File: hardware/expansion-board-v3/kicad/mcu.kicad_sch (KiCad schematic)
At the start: 31 parts, among them J4 USB-C_16P, SW1 RESET短接焊盘, SW2 BOOTSEL短接焊盘, U8 RP2040, U9 W25Q128JVSIQ, Y1 12MHz

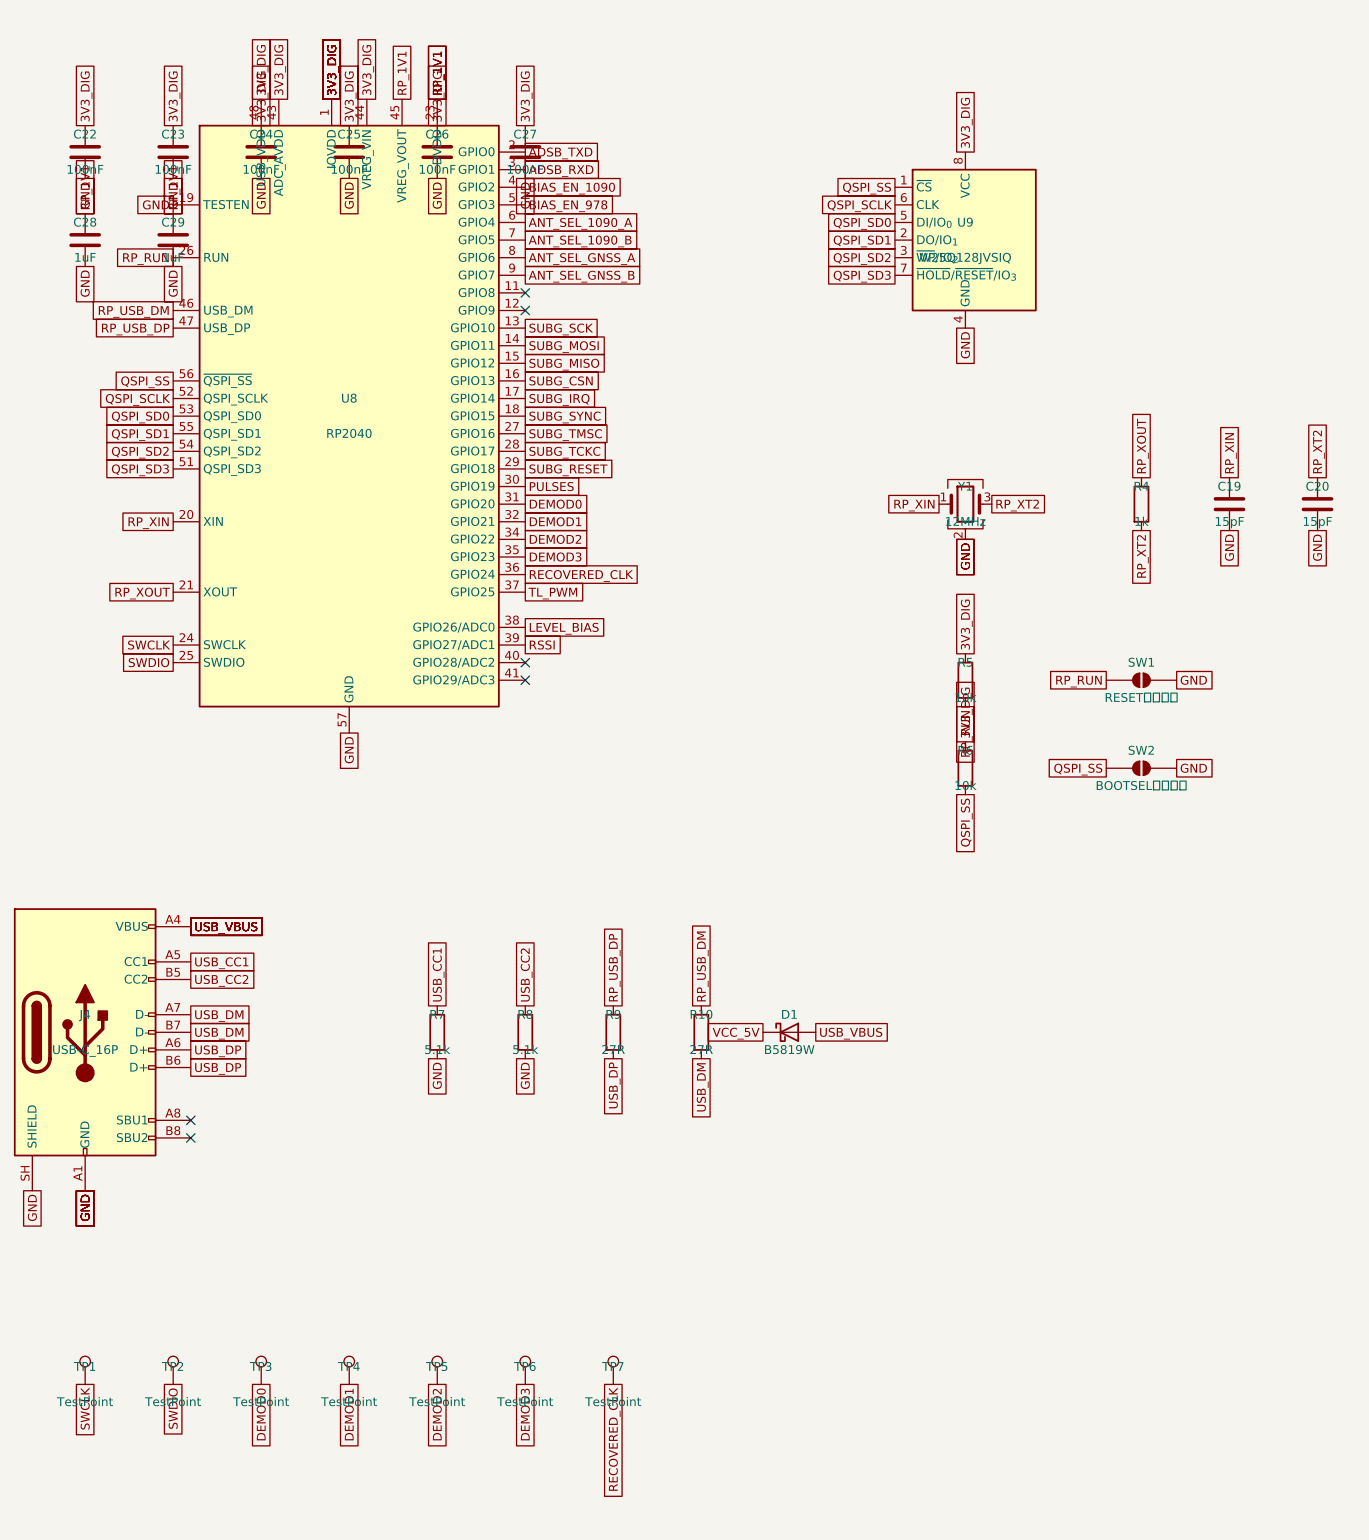
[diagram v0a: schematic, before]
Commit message: feat(v3): backport V4 fixes into a clean V3.9 candidate (phases A-D)
Builds the V3.9 candidate from the V3.8 master rather than from the
working-tree intermediate. The intermediate had the 14 audit parts and a
cleared back side, but had lost 24 board-level silkscreen strings and all
four named RF zones - tools/rebuild.sh starts with gen_pcb.py, which calls
pcbnew.NewBoard(), and neither gr_text nor named zones live in
PLACEMENT.py or ROUTES.json, so every run drops them. The master is the
opposite: intact silkscreen and zones, missing only components. Adding
components back is enumerable (14 designators); restoring 24 silkscreen
strings with correct position, layer, size and mirroring is not.

Coordinates are transplanted from the intermediate, so nothing is
re-placed by hand. What that does cost is copper: the master was routed
without these parts, and 13 of the 18 land on existing tracks. Ripping
those out plus the resulting dangling chains removes 176 segments and 26
vias against the master's 1620/377 - all of it folded into phase E, which
was going to be manual routing anyway. Re-placing 13 parts on a fully
routed board would have been worse; C82-C86 are RP2040 local decouplers
that must stay next to the die, which is exactly how V4.3 ended up with
its 30 mm detour.

Phase B removes the AD8319 experimental branch (U13, R20, DET_TADJ). The
"directional error" turned out to reach into the generators, not just
prose - five places, of which two would have produced wrong hardware:

    gen_bom_smt.py   SKIP_REF = {"U14"}   the only detector excluded
                                          from the pick-and-place BOM
    gen_bom.py       ORDERED listed "AD8313ARMZ(备,二选一)", a suffixed
                     string that never matched the netlist value, so the
                     part had never once been classified

Ordering the V3.8 BOM as it stood would have produced a board whose 1090
receive chain has no detector at all. Phase B's hard criterion now holds:
excluding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
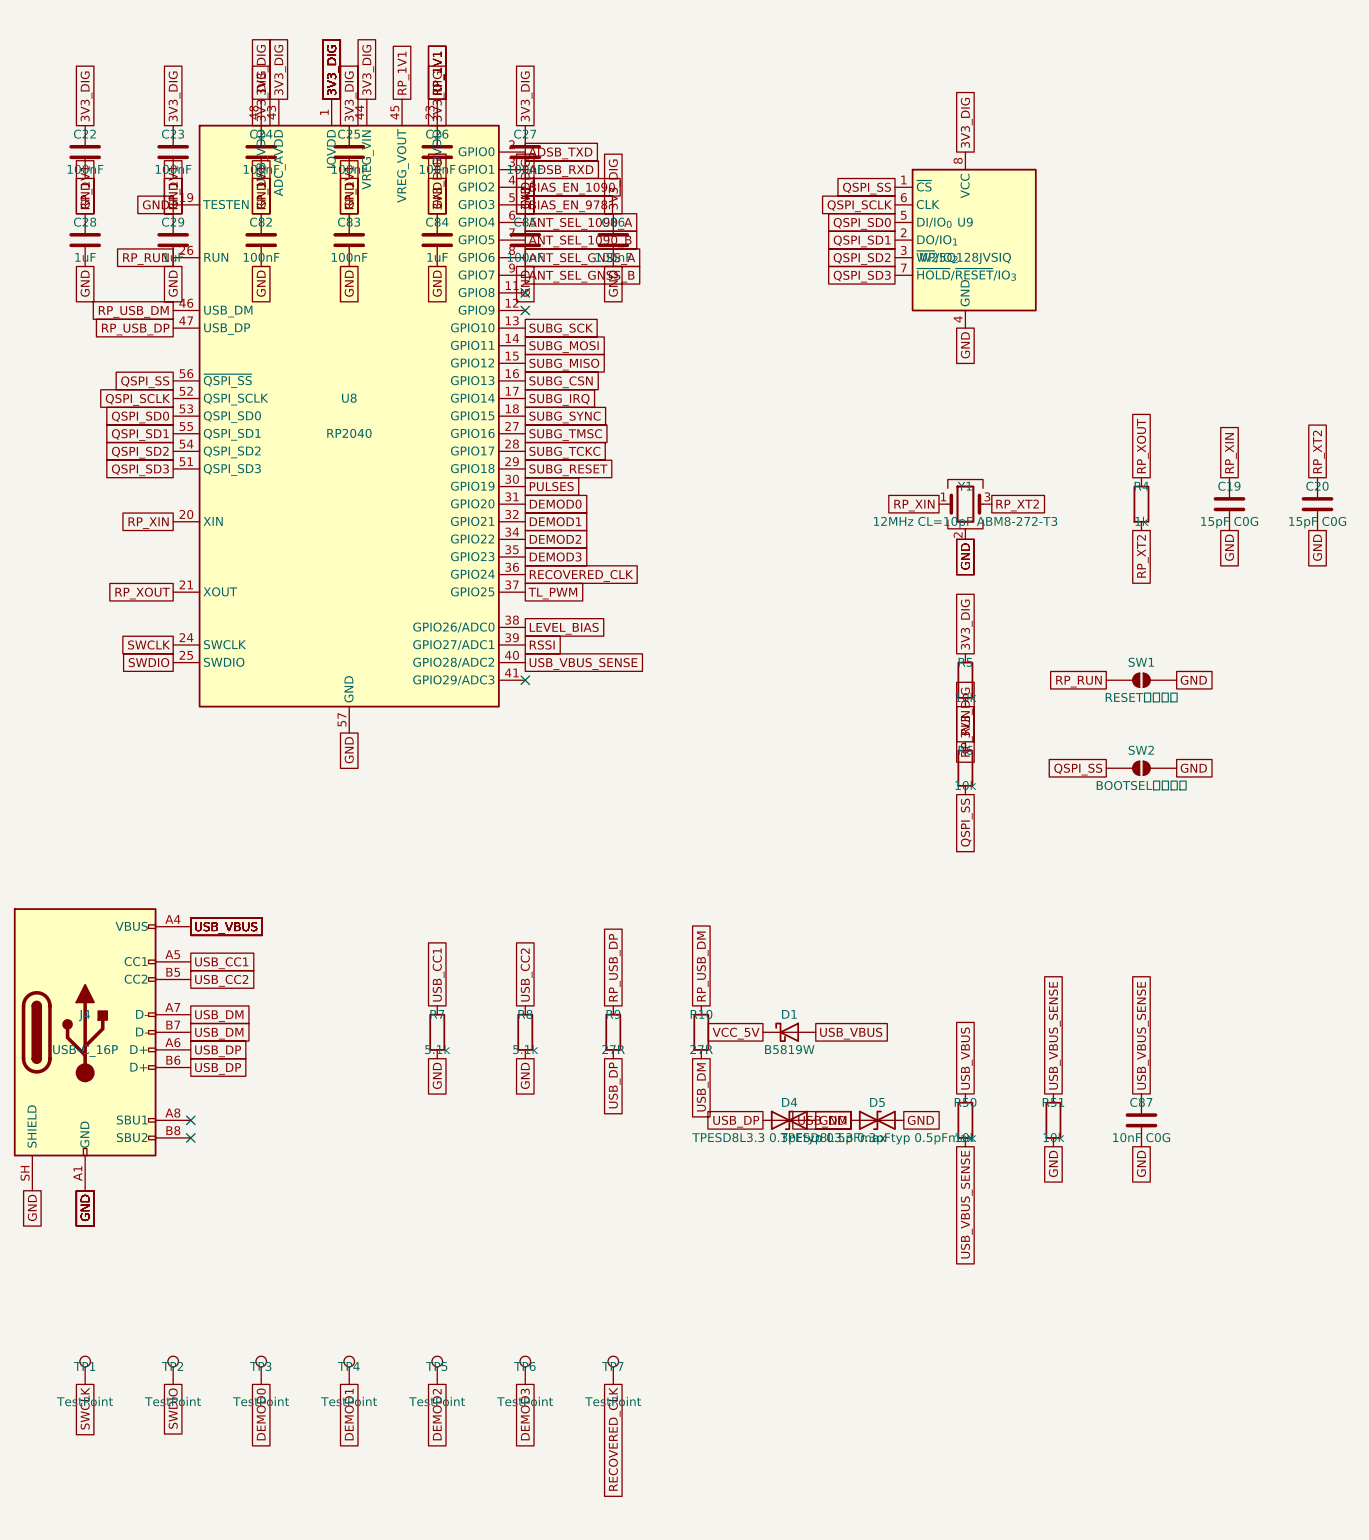
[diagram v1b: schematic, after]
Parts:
- added C82, C83, C85, C86: 100nF, Capacitor_SMD:C_0402_1005Metric, symbol Device:C
- added C84: 1uF, Capacitor_SMD:C_0402_1005Metric, symbol Device:C
- added C87: 10nF C0G, Capacitor_SMD:C_0603_1608Metric, symbol Device:C
- added D4, D5: TPESD8L3.3 0.3pFtyp 0.5pFmax, Diode_SMD:D_0402_1005Metric, symbol Device:D_TVS
- added R50, R51: 10k, Resistor_SMD:R_0603_1608Metric, symbol Device:R
- C19, C20: value 15pF -> 15pF C0G
- Y1: value 12MHz -> 12MHz CL=10pF ABM8-272-T3
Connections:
- net 3V3_DIG: now also C84.1, C85.1, C86.1
- net GND: now also C82.2, C83.2, C84.2, C85.2, C86.2, C87.2, D4.2 (A2), D5.2 (A2), R51.2
- net RP_1V1: now also C82.1, C83.1
- net USB_DM: now also D5.1 (A1)
- net USB_DP: now also D4.1 (A1)
- net USB_VBUS: now also R50.1
- net USB_VBUS_SENSE: now reaches U8.40 (GPIO28/ADC2)
- net USB_VBUS_SENSE: now also C87.1, R50.2, R51.1
- no-connect marks 6 -> 5
